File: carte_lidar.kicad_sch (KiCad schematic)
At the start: 27 parts, among them J1 Conn_01x03_Pin, J2 Conn_01x02_Pin, J3 Conn_01x05_Socket, J4 Conn_01x02, J5 Conn_01x08_Pin, P1 USB_C_Plug_USB2.0, U1 TPS54302, U2 RP2040, U3 CH340C

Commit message: v1
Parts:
- removed J5: Conn_01x08_Pin, Connector_PinHeader_1.00mm:PinHeader_1x08_P1.00mm_Vertical, symbol Connector:Conn_01x08_Pin
- removed P1: USB_C_Plug_USB2.0, symbol Connector:USB_C_Plug_USB2.0
- removed U2: RP2040, Package_DFN_QFN:QFN-56-1EP_7x7mm_P0.4mm_EP3.2x3.2mm, symbol MCU_RaspberryPi:RP2040
- removed U3: CH340C, Package_SO:SOIC-16_3.9x9.9mm_P1.27mm, symbol Interface_USB:CH340C
- added J5: Conn_01x04_Socket, Connector_PinSocket_2.54mm:PinSocket_1x04_P2.54mm_Vertical, symbol Connector:Conn_01x04_Socket
- added R5: 330R, Resistor_SMD:R_0603_1608Metric, symbol Device:R
- added U2: Pico, MCU_RaspberryPi_and_Boards:RPi_Pico_SMD_TH, symbol MCU_RaspberryPi_and_Boards:Pico
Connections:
- net 5V: now also J1.1 (Pin_1), J3.1 (Pin_1), J5.1 (Pin_1), U2.39 (VSYS), U2.40 (VBUS)
- net AU: now also U2.1 (GPIO0)
- net GND: now also J1.2 (Pin_2), J3.4 (Pin_4), J5.2 (Pin_2), U2.13 (GND), U2.18 (GND), U2.23 (GND), U2.28 (GND), U2.3 (GND), U2.38 (GND), U2.42 (GND), U2.8 (GND)
- net led: now reaches J1.3 (Pin_3)
- net led: now also R5.1
- net lidar_tx: now reaches J3.2 (Pin_2)
- net lidar_tx: now also U2.17 (GPIO13)
- net lidar_rx: now reaches J3.3 (Pin_3)
- net lidar_rx: now also U2.16 (GPIO12)
- net motoct: now reaches J3.5 (Pin_5)
- net motoct: now also U2.15 (GPIO11)
- new net: R5.2, U2.6 (GPIO4)
- new net scl: J5.3 (Pin_3), U2.12 (GPIO9)
- new net sda: J5.4 (Pin_4), U2.11 (GPIO8)
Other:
- moved on the sheet: J3, J4, R3, R4

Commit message: update all
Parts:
- removed C1, C2: 10µF 50V, Capacitor_SMD:C_1206_3216Metric, symbol Device:C
- removed C10, C6, C7, C8, C9: 22µF 25V, Capacitor_SMD:C_0805_2012Metric, symbol Device:C
- removed C3: 100nF 50V, Capacitor_SMD:C_0805_2012Metric, symbol Device:C
- removed C4: 100nF 50V, Capacitor_SMD:C_0402_1005Metric, symbol Device:C
- removed C5: 150pF 50V, Capacitor_SMD:C_1206_3216Metric, symbol Device:C
- removed J2: Conn_01x02_Pin, Connector_AMASS:AMASS_XT30U-F_1x02_P5.0mm_Vertical, symbol Connector:Conn_01x02_Pin
- removed J5: Conn_01x04_Socket, Connector_PinSocket_2.54mm:PinSocket_1x04_P2.54mm_Vertical, symbol Connector:Conn_01x04_Socket
- removed L1: PSPMAQ0605H-150M-ANP, 7Robot_lib:Prod_Tech_7.1x6.6mm, symbol Device:L
- removed R1: 100k, Resistor_SMD:R_0603_1608Metric, symbol Device:R
- removed R2: 13.3k, Resistor_SMD:R_0603_1608Metric, symbol Device:R
- removed U1: TPS54302, Package_TO_SOT_SMD:SOT-23-6, symbol Regulator_Switching:TPS54302
- removed U2: Pico, MCU_RaspberryPi_and_Boards:RPi_Pico_SMD_TH, symbol MCU_RaspberryPi_and_Boards:Pico
- added C21, C24, C25, C27: 0.1uF 10V, Capacitor_SMD:C_0402_1005Metric, symbol Device:C
- added C23: 2.2nF 10V, Capacitor_SMD:C_0402_1005Metric, symbol Device:C
- added C26: 1uF 10V, Capacitor_SMD:C_0402_1005Metric, symbol Device:C
- added C28: 220nF 16V, Capacitor_SMD:C_0402_1005Metric, symbol Device:C
- added J5: Conn_01x02_Pin, Connector_PinHeader_2.54mm:PinHeader_1x02_P2.54mm_Vertical, symbol Connector:Conn_01x02_Pin
- added R16: 10k, Capacitor_SMD:C_0402_1005Metric, symbol Device:R
- added R6: 1k, Resistor_SMD:R_0402_1005Metric, symbol Device:R
- added R7: 100k, Resistor_SMD:R_0402_1005Metric, symbol Device:R
- added SW1: SW_Push, Button_Switch_SMD:SW_SPST_B3U-1000P, symbol Switch:SW_Push
- added U2: RP2040, Package_DFN_QFN:QFN-56-1EP_7x7mm_P0.4mm_EP3.2x3.2mm_ThermalVias, symbol MCU_RaspberryPi:RP2040
- added U3: W25Q128JVS, Package_SO:SOIC-8_5.23x5.23mm_P1.27mm, symbol Memory_Flash:W25Q128JVS
- added U7: MPU-6000, Sensor_Motion:InvenSense_QFN-24_4x4mm_P0.5mm, symbol Sensor_Motion:MPU-6000
- added X1: S2D12.000000B20F30T, Oscillator:Oscillator_SMD_ECS_2520MV-xxx-xx-4Pin_2.5x2.0mm, symbol Oscillator:ECS-2520MV-xxx-xx
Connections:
- net AU: now also U2.37 (GPIO25)
- net GND: now also C21.2, C23.2, C24.2, C25.2, C26.2, C27.2, C28.2, J5.2 (Pin_2), SW1.1, U2.19 (TESTEN), U2.57 (GND), U3.4 (GND), U7.1 (CLKIN), U7.11 (FSYNC), U7.18 (GND), U7.6 (AUX_DA), U7.7 (AUX_CL), X1.2 (GND)
- net led: now also R5.2, U2.15 (GPIO12); no longer J1.3 (Pin_3), R5.1
- net lidar_rx: now also U2.32 (GPIO21)
- net lidar_tx: now also U2.31 (GPIO20)
- net motoct: now also U2.30 (GPIO19)
- net 5V renamed +5V
- net +5V: no longer R4.1
- new net: C23.1, U7.20 (CPOUT)
- new net: J1.3 (Pin_3), R5.1
- new net: R16.2, U2.26 (RUN)
- new net: C26.1, U2.45 (VREG_VOUT)
- new net: U2.51 (QSPI_SD3), U3.7 (IO3)
- new net: U2.52 (QSPI_SCLK), U3.6 (CLK)
- new net: U2.53 (QSPI_SD0), U3.5 (DI(IO0))
- new net: U2.54 (QSPI_SD2), U3.3 (IO2)
- new net: U2.55 (QSPI_SD1), U3.2 (DO(IO1))
- new net: R6.1, R7.1, U2.56 (QSPI_SS), U3.1 (~{CS})
- new net: J5.1 (Pin_1), R6.2, SW1.2
- new net: C21.1, U7.10 (REGOUT)
- new net +1.1V: C25.1, C27.1, U2.23 (DVDD), U2.50 (DVDD)
- new net +3V3: C24.1, C28.1, R16.1, R4.1, R7.2, U2.1 (IOVDD), U2.10 (IOVDD), U2.22 (IOVDD), U2.33 (IOVDD), U2.42 (IOVDD), U2.43 (ADC_AVDD), U2.44 (VREG_IN), U2.48 (USB_VDD), U2.49 (IOVDD), U3.8 (VCC), U7.13 (VDD), X1.4 (VDD)
- new net BAT_SENSE: U2.38 (GPIO26_ADC0)
- new net CSn: U2.7 (GPIO5), U7.8 (~{CS})
- new net Clk_12MHz: U2.24 (SWCLK), X1.3 (OUT)
- new net INT: U7.12 (INT)
- new net MISO: U2.6 (GPIO4), U7.9 (AD0/MISO)
- new net MOSI: U2.9 (GPIO7), U7.24 (SDA/MOSI)
- new net SCLK: U2.8 (GPIO6), U7.23 (SCL/SCLK)
- new net USB_N: U2.46 (USB_DM)
- new net USB_P: U2.47 (USB_DP)
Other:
- added sheet USB (usb.kicad_sch)
- added sheet power (power.kicad_sch)
- note added: "Each close to a DVDD pin"
- moved on the sheet: H1, H2, H3, J1, J3, J4, R3, R4

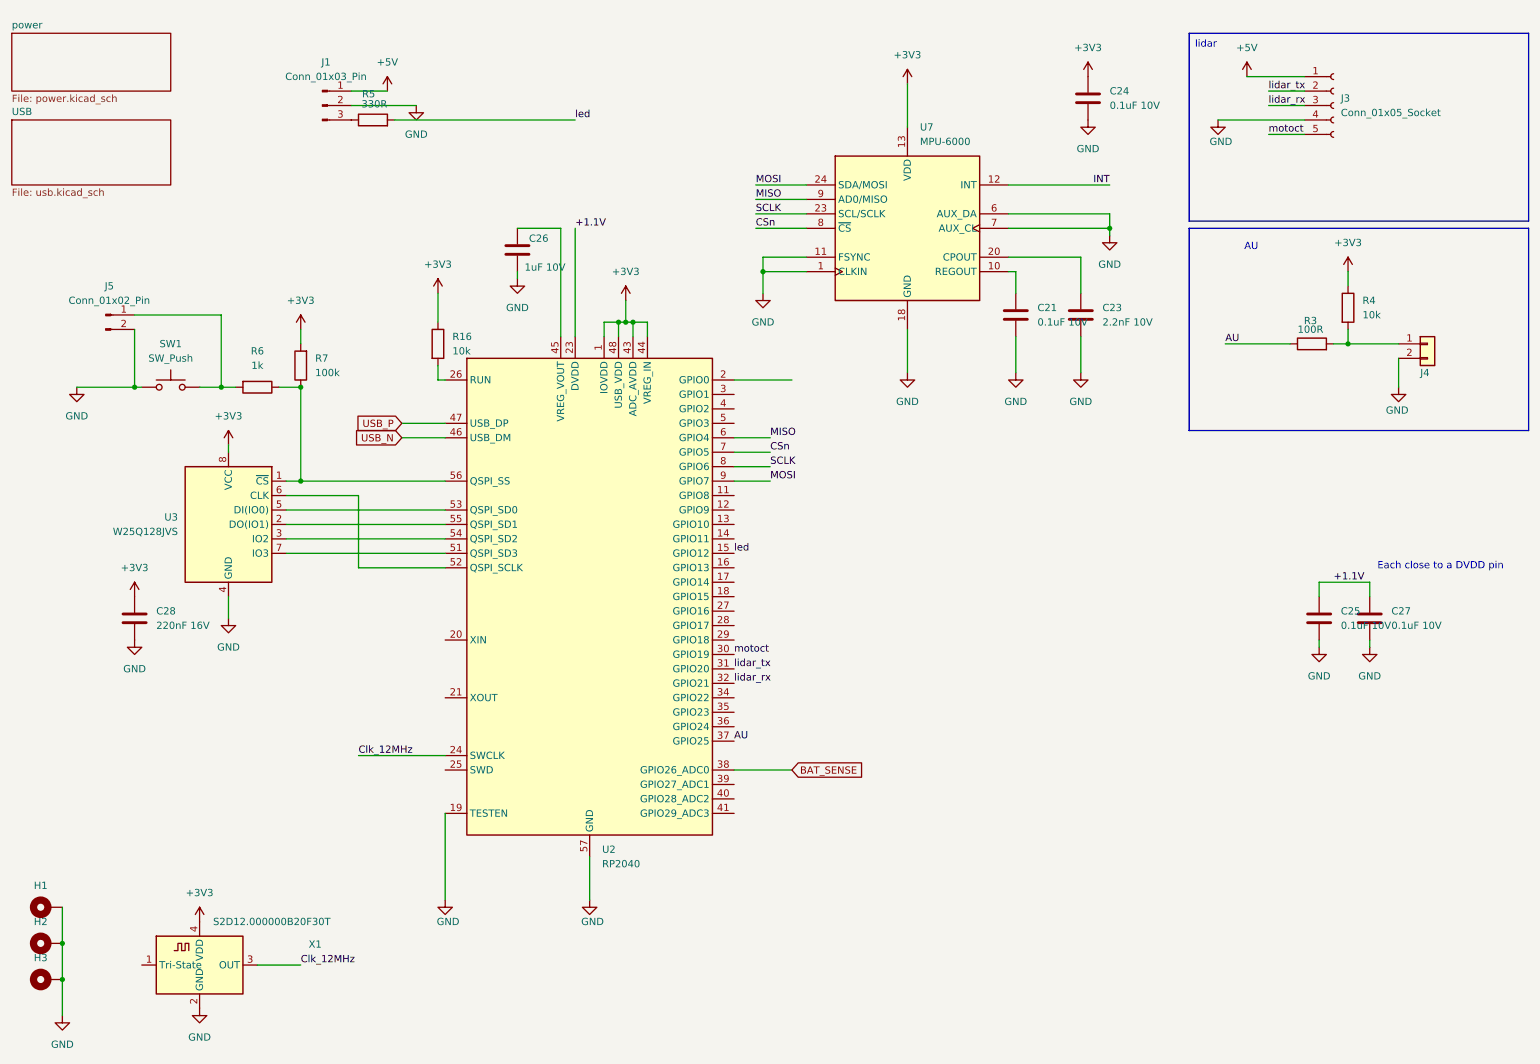
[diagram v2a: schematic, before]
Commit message: add ethernet in schematic
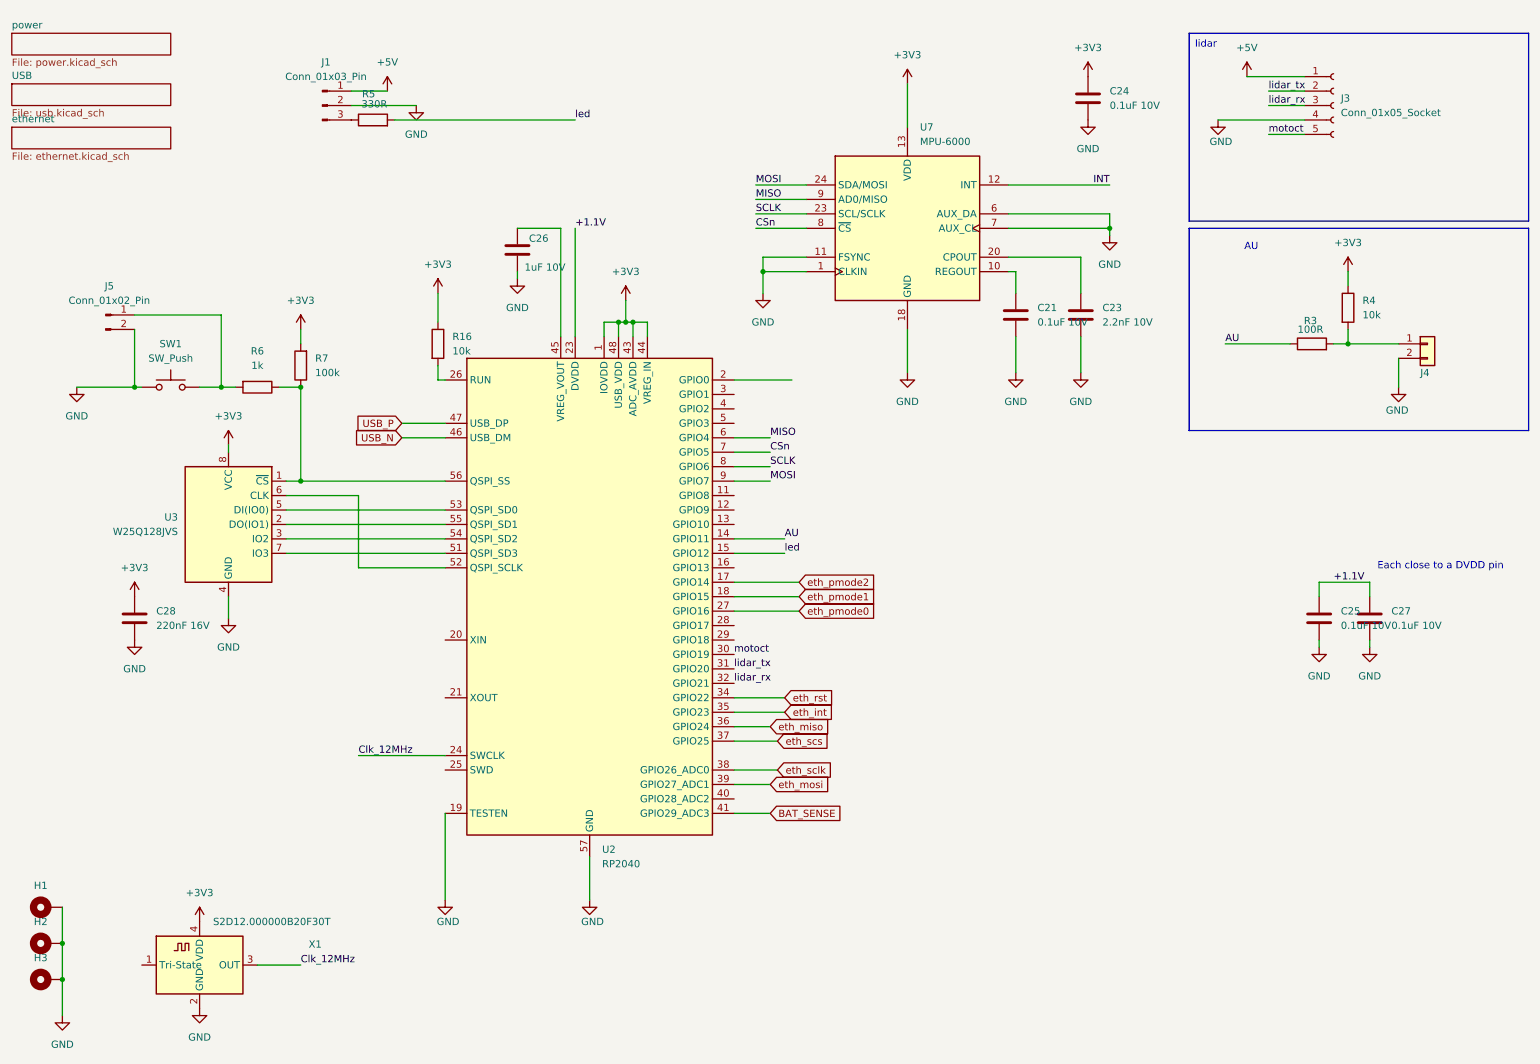
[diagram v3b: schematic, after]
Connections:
- net AU: now also U2.14 (GPIO11); no longer U2.37 (GPIO25)
- net BAT_SENSE: now also U2.41 (GPIO29_ADC3); no longer U2.38 (GPIO26_ADC0)
- net eth_pmode2: now reaches U2.17 (GPIO14)
- net eth_pmode1: now reaches U2.18 (GPIO15)
- net eth_pmode0: now reaches U2.27 (GPIO16)
- net eth_rst: now reaches U2.34 (GPIO22)
- net eth_int: now reaches U2.35 (GPIO23)
- net eth_miso: now reaches U2.36 (GPIO24)
- net eth_mosi: now reaches U2.39 (GPIO27_ADC1)
- new net eth_sclk: U2.38 (GPIO26_ADC0)
- new net eth_scs: U2.37 (GPIO25)
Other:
- added sheet ethernet (ethernet.kicad_sch)

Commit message: update all
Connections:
- net tof3: now reaches U2.16 (GPIO13)
- net sda: now reaches U2.2 (GPIO0)
- net scl: now reaches U2.3 (GPIO1)
- net tof2: now reaches U2.4 (GPIO2)
- net tof1: now reaches U2.5 (GPIO3)
- net eth_pmode0: no longer names the net of U2.27 (GPIO16)
- net eth_pmode1: no longer names the net of U2.18 (GPIO15)
- net eth_pmode2: no longer names the net of U2.17 (GPIO14)
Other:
- added sheet tof (tof.kicad_sch)
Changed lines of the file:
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@@
 	(wire
 		(pts
-			(xy 152.4 118.11) (xy 140.97 118.11)
-		)
-		(stroke
-			(width 0)
-			(type default)
-		)
-	)
-	(wire
-		(pts
 			(xy 147.32 138.43) (xy 140.97 138.43)
 		)
@@
 	(wire
 		(pts
+			(xy 157.48 97.79) (xy 140.97 97.79)
+		)
+		(stroke
+			(width 0)
+			(type default)
+		)
+	)
+	(wire
+		(pts
 			(xy 190.5 58.42) (xy 189.23 58.42)
 		)
@@
 	(wire
 		(pts
+			(xy 157.48 85.09) (xy 140.97 85.09)
+		)
+		(stroke
+			(width 0)
+			(type default)
+		)
+	)
+	(wire
+		(pts
 			(xy 118.11 69.85) (xy 118.11 67.31)
 		)
@@
 	(wire
 		(pts
-			(xy 152.4 113.03) (xy 140.97 113.03)
-		)
-		(stroke
-			(width 0)
-			(type default)
-		)
-	)
-	(wire
-		(pts
 			(xy 252.73 123.19) (xy 252.73 124.46)
 		)
@@
 	(wire
 		(pts
-			(xy 152.4 115.57) (xy 140.97 115.57)
-		)
-		(stroke
-			(width 0)
-			(type default)
-		)
-	)
-	(wire
-		(pts
 			(xy 110.49 69.85) (xy 110.49 50.8)
 		)
@@
 	(wire
 		(pts
+			(xy 151.13 110.49) (xy 140.97 110.49)
+		)
+		(stroke
+			(width 0)
+			(type default)
+		)
+	)
+	(wire
+		(pts
 			(xy 62.23 107.95) (xy 90.17 107.95)
 		)
@@
 	(wire
 		(pts
+			(xy 157.48 82.55) (xy 140.97 82.55)
+		)
+		(stroke
+			(width 0)
+			(type default)
+		)
+	)
+	(wire
+		(pts
 			(xy 113.03 69.85) (xy 113.03 50.8)
 		)
@@
 	(wire
 		(pts
+			(xy 151.13 80.01) (xy 140.97 80.01)
+		)
+		(stroke
+			(width 0)
+			(type default)
+		)
+	)
+	(wire
+		(pts
 			(xy 62.23 95.25) (xy 64.77 95.25)
 		)
@@
 		)
 	)
-	(global_label "eth_rst"
+	(global_label "tof3"
 		(shape input)
-		(at 149.86 133.35 0)
+		(at 151.13 110.49 0)
 		(fields_autoplaced yes)
 		(effects
@@
 		)
 		(property "Intersheetrefs" "${INTERSHEET_REFS}"
-			(at 159.3161 133.35 0)
+			(at 157.9251 110.49 0)
 			(effects
 				(font
@@
 		)
 	)
-	(global_label "BAT_SENSE"
+	(global_label "tof2"
 		(shape input)
-		(at 147.32 153.67 0)
+		(at 157.48 82.55 0)
 		(fields_autoplaced yes)
 		(effects
@@
 		)
 		(property "Intersheetrefs" "${INTERSHEET_REFS}"
-			(at 160.6465 153.67 0)
+			(at 164.2751 82.55 0)
 			(effects
 				(font
@@
 		)
 	)
-	(global_label "eth_int"
+	(global_label "sda"
 		(shape input)
-		(at 149.86 135.89 0)
+		(at 151.13 77.47 0)
 		(fields_autoplaced yes)
 		(effects
@@
 		)
 		(property "Intersheetrefs" "${INTERSHEET_REFS}"
-			(at 159.2556 135.89 0)
+			(at 157.4413 77.47 0)
 			(effects
 				(font
@@
 		)
 	)
-	(global_label "eth_scs"
+	(global_label "eth_rst"
 		(shape input)
-		(at 148.59 140.97 0)
+		(at 149.86 133.35 0)
 		(fields_autoplaced yes)
 		(effects
@@
 		)
 		(property "Intersheetrefs" "${INTERSHEET_REFS}"
-			(at 158.6509 140.97 0)
+			(at 159.3161 133.35 0)
 			(effects
 				(font
@@
 		)
 	)
-	(global_label "eth_mosi"
+	(global_label "BAT_SENSE"
 		(shape input)
-		(at 147.32 148.59 0)
+		(at 147.32 153.67 0)
 		(fields_autoplaced yes)
 		(effects
@@
 		)
 		(property "Intersheetrefs" "${INTERSHEET_REFS}"
-			(at 158.7113 148.59 0)
+			(at 160.6465 153.67 0)
 			(effects
 				(font
@@
 		)
 	)
-	(global_label "eth_sclk"
+	(global_label "tof1"
 		(shape input)
-		(at 148.59 146.05 0)
+		(at 157.48 85.09 0)
 		(fields_autoplaced yes)
 		(effects
@@
 		)
 		(property "Intersheetrefs" "${INTERSHEET_REFS}"
-			(at 159.3161 146.05 0)
+			(at 164.2751 85.09 0)
 			(effects
 				(font
@@
 		)
 	)
-	(global_label "USB_P"
+	(global_label "eth_int"
 		(shape input)
-		(at 82.55 85.09 180)
+		(at 149.86 135.89 0)
 		(fields_autoplaced yes)
 		(effects
@@
 				(size 1.27 1.27)
 			)
-			(justify right)
+			(justify left)
 		)
 		(property "Intersheetrefs" "${INTERSHEET_REFS}"
-			(at 73.5172 85.09 0)
+			(at 159.2556 135.89 0)
 			(effects
 				(font
 					(size 1.27 1.27)
 				)
-				(justify right)
+				(justify left)
+				(hide yes)
+			)
+		)
+	)
+	(global_label "eth_scs"
+		(shape input)
+		(at 148.59 140.97 0)
+		(fields_autoplaced yes)
+		(effects
+			(font
+				(size 1.27 1.27)
+			)
+			(justify left)
+		)
+		(property "Intersheetrefs" "${INTERSHEET_REFS}"
+			(at 158.6509 140.97 0)
+			(effects
+				(font
+					(size 1.27 1.27)
+				)
+				(justify left)
 				(hide yes)
 			)
 		)
 	)
-	(global_label "eth_pmode0"
+	(global_label "scl"
 		(shape input)
-		(at 152.4 118.11 0)
+		(at 151.13 80.01 0)
 		(fields_autoplaced yes)
 		(effects
@@
 		)
 		(property "Intersheetrefs" "${INTERSHEET_REFS}"
-			(at 166.7545 118.11 0)
+			(at 156.8971 80.01 0)
 			(effects
 				(font
@@
 		)
 	)
-	(global_label "eth_pmode2"
+	(global_label "eth_mosi"
 		(shape input)
-		(at 152.4 113.03 0)
+		(at 147.32 148.59 0)
 		(fields_autoplaced yes)
 		(effects
@@
 		)
 		(property "Intersheetrefs" "${INTERSHEET_REFS}"
-			(at 166.7545 113.03 0)
+			(at 158.7113 148.59 0)
 			(effects
 				(font
@@
 		)
 	)
-	(global_label "eth_pmode1"
+	(global_label "eth_sclk"
 		(shape input)
-		(at 152.4 115.57 0)
+		(at 148.59 146.05 0)
 		(fields_autoplaced yes)
 		(effects
@@
 		)
 		(property "Intersheetrefs" "${INTERSHEET_REFS}"
-			(at 166.7545 115.57 0)
+			(at 159.3161 146.05 0)
 			(effects
 				(font
@@
 		)
 	)
+	(global_label "USB_P"
+		(shape input)
+		(at 82.55 85.09 180)
+		(fields_autoplaced yes)
+		(effects
+			(font
+				(size 1.27 1.27)
+			)
+			(justify right)
+		)
+		(property "Intersheetrefs" "${INTERSHEET_REFS}"
+			(at 73.5172 85.09 0)
+			(effects
+				(font
+					(size 1.27 1.27)
+				)
+				(justify right)
+				(hide yes)
+			)
+		)
+	)
 	(global_label "USB_N"
 		(shape input)
@@
 				)
 			)
+		)
+	)
+	(sheet
+		(at 13.97 40.64)
+		(size 27.94 5.08)
+		(fields_autoplaced yes)
+		(stroke
+			(width 0.1524)
+			(type solid)
+		)
+		(fill
+			(color 0 0 0 0.0000)
+		)
+		(property "Sheetname" "tof"
+			(at 13.97 39.9284 0)
+			(effects
+				(font
+					(size 1.27 1.27)
+				)
+				(justify left bottom)
+			)
+		)
+		(property "Sheetfile" "tof.kicad_sch"
+			(at 13.97 46.3046 0)
+			(effects
+				(font
+					(size 1.27 1.27)
+				)
+				(justify left top)
+			)
+		)
+		(instances
+			(project "carte_lidar"
+				(path "/8c7c486d-228e-4b66-b6d5-0b7cf34b4d2b"
+					(page "5")
+				)
+			)

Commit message: update
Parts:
- added C31, C32, C33, C34, C35, C36: 1uF 6.3V, Capacitor_SMD:C_0402_1005Metric, symbol Device:C
- C26: value 1uF 10V -> 1uF 6.3V
- U2: footprint Package_DFN_QFN:QFN-56-1EP_7x7mm_P0.4mm_EP3.2x3.2mm_ThermalVias -> Package_DFN_QFN:QFN-56-1EP_7x7mm_P0.4mm_EP3.2x3.2mm
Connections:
- net +3V3: now also C31.1, C32.1, C33.1, C34.1, C35.1, C36.1
- net GND: now also C31.2, C32.2, C33.2, C34.2, C35.2, C36.2
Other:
- note added: "Each close to a IO_VDD pin"
- moved on the sheet: R5
